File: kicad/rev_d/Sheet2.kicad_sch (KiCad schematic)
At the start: 216 parts, among them J10 vg_old, J5 external clock, J6 JUMPER, J8 JUMPER, J9 JUMPER, Q2 QUARTZ, Q3 QUARTZ32768, U1 74HCT1G04, X10 ST-214C, X11 KEYB-MOUSE, X12 IDC20, X13 USB_C, X14 AAFP/AC97 audio, X15 PLB2-2, X16 PLB1-4I, X17 PLB1-4I, X18 PLB1-4I, X19 AVR pgm conn, X20 PLB1-4I, X4 IDC10M, X5 IDC10M, X6 RS232_9

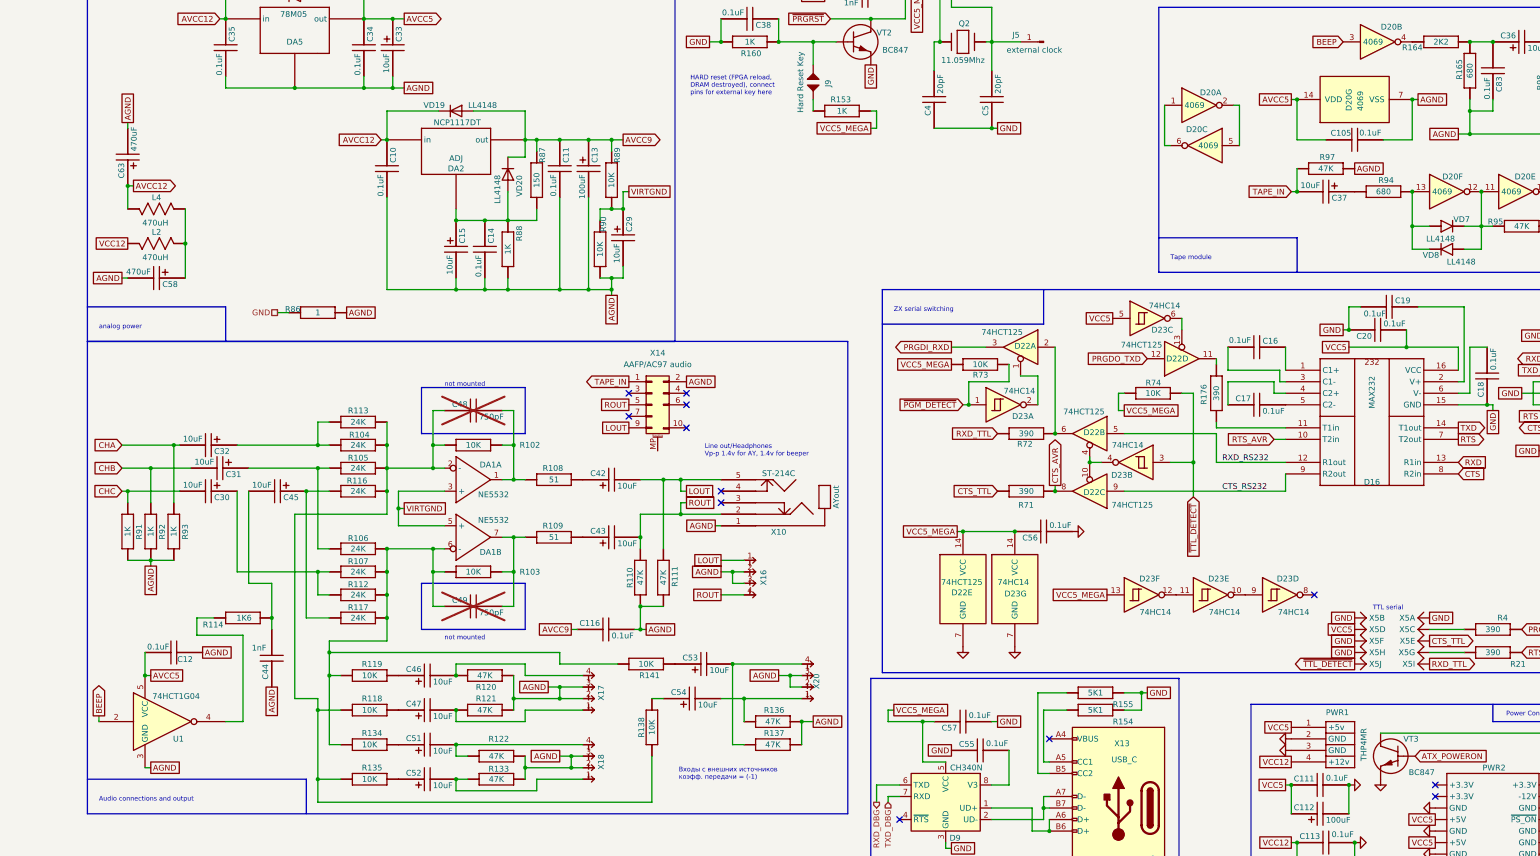
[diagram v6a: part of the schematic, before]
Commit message: pentevo: rev D: remove AGND, use GND instead
git-svn-id: svn://localhost/local-pentevo@1211 c6c76956-fad2-4150-a3a9-ea0a427205ba
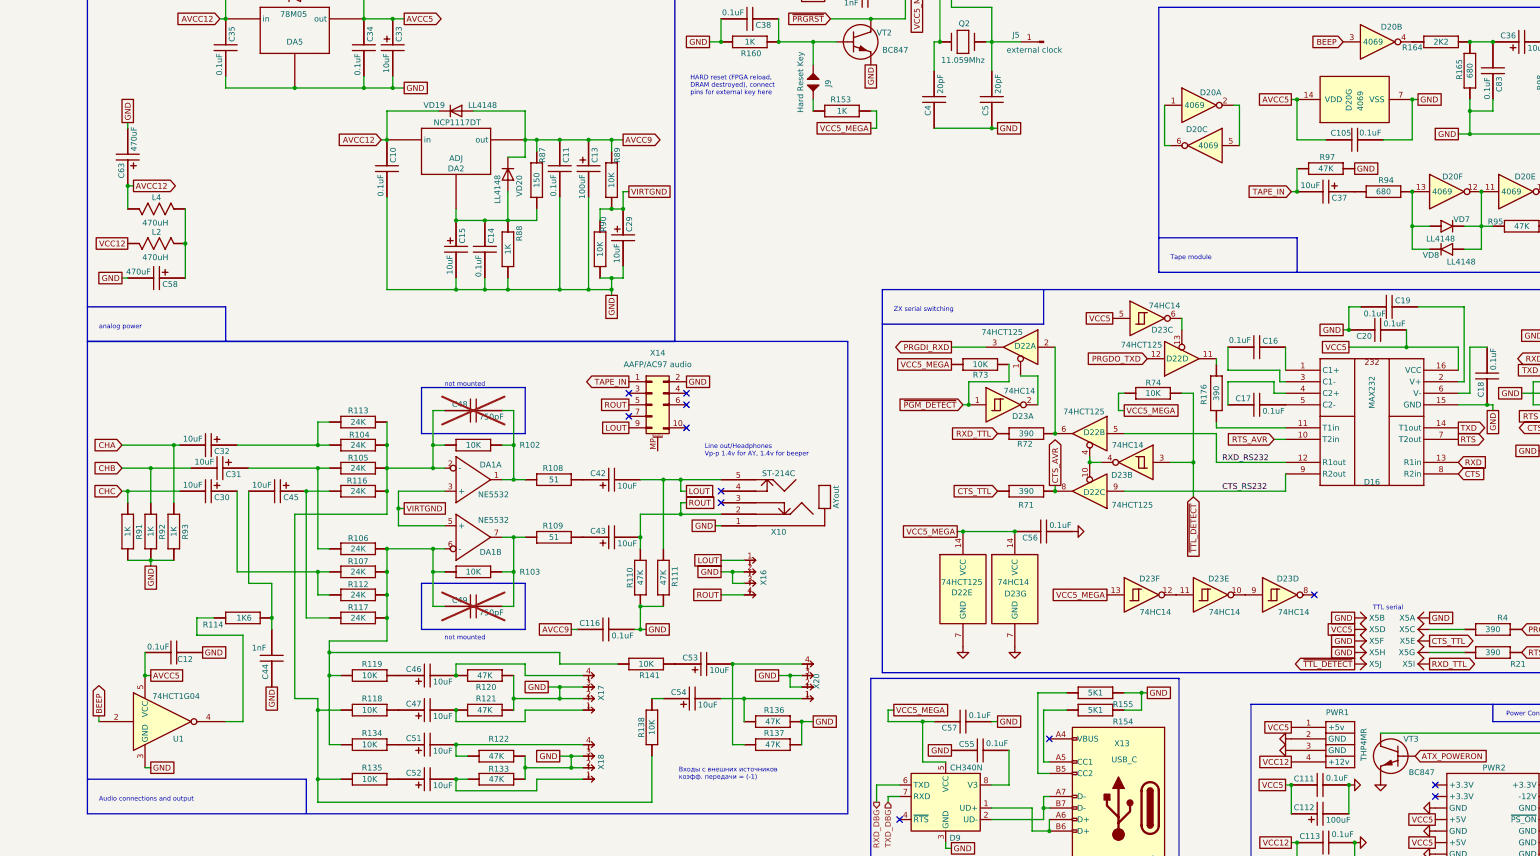
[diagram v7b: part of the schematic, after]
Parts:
- removed R86: 1, R-CHIP, symbol eva-altium-import:Sheet2_0_RESCHIP
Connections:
- net AGND is gone; now on net GND: C10.2, C105.2, C11.2, C116.2, C12.1, C13.2, C14.2, C15.2, C29.2, C33.2, C34.2, C35.2, C44.1, C58.2, C63.2, C83.1, D20.7 (VSS), DA5.2, R110.1 (i/o), R111.1 (i/o), R120.1 (i/o), R121.1 (i/o), R122.1 (i/o), R133.1 (i/o), R136.1 (i/o), R137.1 (i/o), R165.2 (i/o1), R88.1 (i/o), R90.1 (i/o), R91.1 (i/o), R92.1 (i/o), R93.1 (i/o), R97.1 (i/o), R98.1 (i/o), U1.3 (GND), X10.1, X14.2 (Pin_2), X15.2, X15.4 (2), X16.2 (I/O2), X16.3 (I/O3), X17.2 (I/O2), X17.3 (I/O3), X18.2 (I/O2), X18.3 (I/O3), X20.2 (I/O2), X20.3 (I/O3)
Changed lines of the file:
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@@
 	(wire
 		(pts
-			(xy 123.19 273.05) (xy 125.73 273.05)
-		)
-		(stroke
-			(width 0)
-			(type default)
-		)
-	)
-	(wire
-		(pts
 			(xy 284.48 88.9) (xy 284.48 96.52)
 		)
@@
 		)
 	)
-	(global_label "AGND"
+	(global_label "GND"
 		(shape passive)
 		(at 185.42 370.84 180)
@@
 		)
 		(property "Intersheetrefs" "${INTERSHEET_REFS}"
-			(at 178.587 370.84 0)
+			(at 179.6756 370.84 0)
 			(effects
 				(font
@@
 		)
 	)
-	(global_label "AGND"
+	(global_label "GND"
 		(shape passive)
 		(at 219.71 320.04 180)
@@
 		)
 		(property "Intersheetrefs" "${INTERSHEET_REFS}"
-			(at 212.877 320.04 0)
+			(at 213.9656 320.04 0)
 			(effects
 				(font
@@
 		)
 	)
-	(global_label "AGND"
+	(global_label "GND"
 		(shape passive)
 		(at 360.68 241.3 0)
@@
 		)
 		(property "Intersheetrefs" "${INTERSHEET_REFS}"
-			(at 367.513 241.3 0)
+			(at 366.4244 241.3 0)
 			(effects
 				(font
@@
 		)
 	)
-	(global_label "AGND"
+	(global_label "GND"
 		(shape passive)
 		(at 374.65 226.06 0)
@@
 		)
 		(property "Intersheetrefs" "${INTERSHEET_REFS}"
-			(at 381.483 226.06 0)
+			(at 380.3944 226.06 0)
 			(effects
 				(font
@@
 		)
 	)
-	(global_label "AGND"
-		(shape passive)
-		(at 138.43 273.05 0)
-		(fields_autoplaced yes)
-		(effects
-			(font
-				(size 1.27 1.27)
-			)
-			(justify left)
-		)
-		(property "Intersheetrefs" "${INTERSHEET_REFS}"
-			(at 145.263 273.05 0)
-			(effects
-				(font
-					(size 1.27 1.27)
-				)
-				(justify left)
-				(hide yes)
-			)
-		)
-	)
 	(global_label "PRGDO_TXD"
 		(shape input)
@@
 		)
 	)
-	(global_label "AGND"
+	(global_label "GND"
 		(shape passive)
 		(at 95.25 328.93 270)
@@
 		)
 		(property "Intersheetrefs" "${INTERSHEET_REFS}"
-			(at 95.25 335.763 90)
+			(at 95.25 334.6744 90)
 			(effects
 				(font
@@
 		)
 	)
-	(global_label "AGND"
+	(global_label "GND"
 		(shape passive)
 		(at 90.17 231.14 90)
@@
 		)
 		(property "Intersheetrefs" "${INTERSHEET_REFS}"
-			(at 90.17 224.307 90)
+			(at 90.17 225.3956 90)
 			(effects
 				(font
@@
 		)
 	)
-	(global_label "AGND"
+	(global_label "GND"
 		(shape passive)
 		(at 220.98 330.2 180)
@@
 		)
 		(property "Intersheetrefs" "${INTERSHEET_REFS}"
-			(at 214.147 330.2 0)
+			(at 215.2356 330.2 0)
 			(effects
 				(font
@@
 		)
 	)
-	(global_label "AGND"
+	(global_label "GND"
 		(shape passive)
 		(at 95.25 373.38 0)
@@
 		)
 		(property "Intersheetrefs" "${INTERSHEET_REFS}"
-			(at 102.083 373.38 0)
+			(at 100.9944 373.38 0)
 			(effects
 				(font
@@
 		)
 	)
-	(global_label "AGND"
+	(global_label "GND"
 		(shape passive)
 		(at 182.88 355.6 180)
@@
 		)
 		(property "Intersheetrefs" "${INTERSHEET_REFS}"
-			(at 176.047 355.6 0)
+			(at 177.1356 355.6 0)
 			(effects
 				(font
@@
 		)
 	)
-	(global_label "AGND"
+	(global_label "GND"
 		(shape passive)
 		(at 204.47 342.9 0)
@@
 		)
 		(property "Intersheetrefs" "${INTERSHEET_REFS}"
-			(at 211.303 342.9 0)
+			(at 210.2144 342.9 0)
 			(effects
 				(font
@@
 		)
 	)
-	(global_label "AGND"
+	(global_label "GND"
 		(shape passive)
 		(at 241.3 363.22 0)
@@
 		)
 		(property "Intersheetrefs" "${INTERSHEET_REFS}"
-			(at 248.133 363.22 0)
+			(at 247.0444 363.22 0)
 			(effects
 				(font
@@
 		)
 	)
-	(global_label "AGND"
+	(global_label "GND"
 		(shape passive)
 		(at 121.92 355.6 270)
@@
 		)
 		(property "Intersheetrefs" "${INTERSHEET_REFS}"
-			(at 121.92 362.433 90)
+			(at 121.92 361.3444 90)
 			(effects
 				(font
@@
 		)
 	)
-	(global_label "AGND"
+	(global_label "GND"
 		(shape passive)
 		(at 383.54 233.68 180)
@@
 		)
 		(property "Intersheetrefs" "${INTERSHEET_REFS}"
-			(at 376.707 233.68 0)
+			(at 377.7956 233.68 0)
 			(effects
 				(font
@@
 		)
 	)
-	(global_label "AGND"
+	(global_label "GND"
 		(shape passive)
 		(at 151.13 223.52 0)
@@
 		)
 		(property "Intersheetrefs" "${INTERSHEET_REFS}"
-			(at 157.963 223.52 0)
+			(at 156.8744 223.52 0)
 			(effects
 				(font
@@
 		)
 	)
-	(global_label "AGND"
+	(global_label "GND"
 		(shape passive)
 		(at 88.9 265.43 180)
@@
 		)
 		(property "Intersheetrefs" "${INTERSHEET_REFS}"
-			(at 82.067 265.43 0)
+			(at 83.1556 265.43 0)
 			(effects
 				(font
@@
 		)
 	)
-	(global_label "AGND"
+	(global_label "GND"
 		(shape passive)
 		(at 106.68 347.98 0)
@@
 		)
 		(property "Intersheetrefs" "${INTERSHEET_REFS}"
-			(at 113.513 347.98 0)
+			(at 112.4244 347.98 0)
 			(effects
 				(font
@@
 		)
 	)
-	(global_label "AGND"
+	(global_label "GND"
 		(shape passive)
 		(at 233.68 353.06 180)
@@
 		)
 		(property "Intersheetrefs" "${INTERSHEET_REFS}"
-			(at 226.847 353.06 0)
+			(at 227.9356 353.06 0)
 			(effects
 				(font
@@
 		)
 	)
-	(global_label "AGND"
+	(global_label "GND"
 		(shape passive)
 		(at 196.85 269.24 270)
@@
 		)
 		(property "Intersheetrefs" "${INTERSHEET_REFS}"
-			(at 196.85 276.073 90)
+			(at 196.85 274.9844 90)
 			(effects
 				(font
@@
 		)
 	)
-	(global_label "AGND"
+	(global_label "GND"
 		(shape passive)
 		(at 213.36 288.29 0)
@@
 		)
 		(property "Intersheetrefs" "${INTERSHEET_REFS}"
-			(at 220.193 288.29 0)
+			(at 219.1044 288.29 0)
 			(effects
 				(font
@@
 		)
 	)
-	(hierarchical_label "GND"
-		(shape passive)
-		(at 123.19 273.05 180)
-		(fields_autoplaced yes)
-		(effects
-			(font
-				(size 1.27 1.27)
-			)
-			(justify right)
-		)
-	)
 	(hierarchical_label "TXD_DBG"
 		(shape input)
@@
 					(unit 1)
 				)
-			)
-		)
-	)
-	(symbol
-		(lib_id "eva-altium-import:Sheet2_0_RESCHIP")
-		(at 125.73 273.05 0)
-		(unit 1)
-		(exclude_from_sim no)
-		(in_bom yes)
-		(on_board yes)
-		(dnp no)
-		(property "Reference" "R86"
-			(at 128.27 273.05 0)
-			(effects
-				(font
-					(size 1.27 1.27)
-				)
-				(justify right bottom)
-			)
-		)
-		(property "Value" "1"
-			(at 132.08 273.05 0)
-			(effects
-				(font
-					(size 1.27 1.27)
-				)
-			)
-		)
-		(property "Footprint" "R-CHIP"
-			(at 125.73 273.05 0)
-			(effects
-				(font
-					(size 1.27 1.27)
-				)
-				(hide yes)
-			)
-		)
-		(property "Datasheet" ""
-			(at 125.73 273.05 0)
-			(effects
-				(font
-					(size 1.27 1.27)
-				)
-				(hide yes)
-			)
-		)
-		(property "Description" "RESCHIP"
-			(at 125.73 273.05 0)
-			(effects
-				(font
-					(size 1.27 1.27)
-				)
-				(hide yes)
-			)
-		)
-		(pin "2"
-		)
-		(pin "1"
-		)
-		(instances
-			(project ""
-				(path "/ab605654-a730-497b-9e09-9b351f74b935/31d5864f-06ec-4c73-9256-780a6880087d"
-					(reference "R86")
-					(unit 1)
-				)

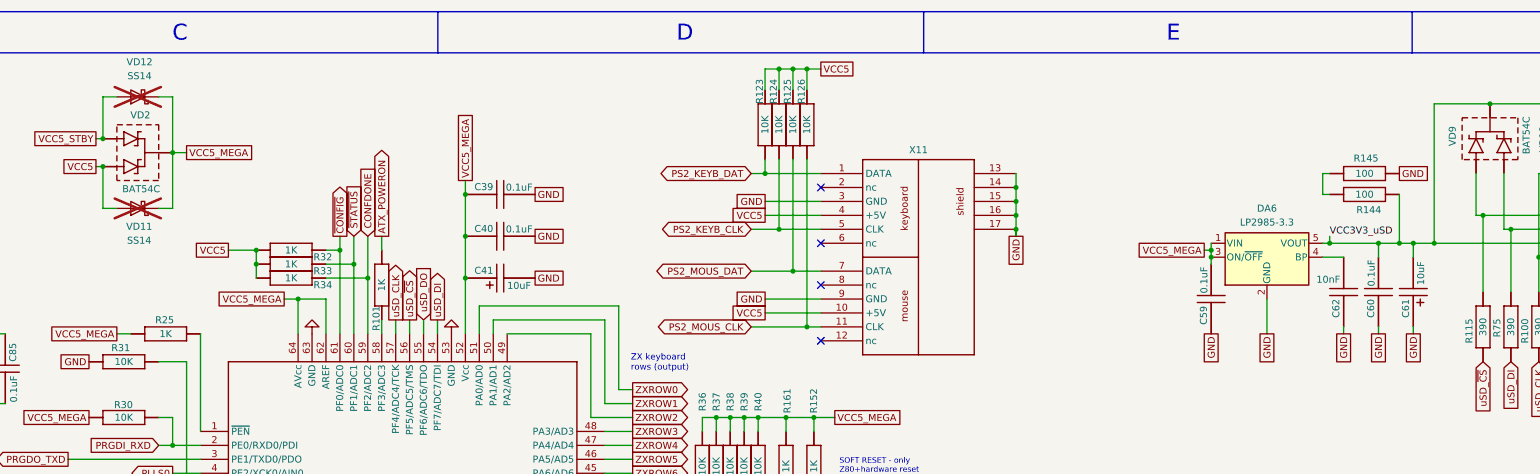
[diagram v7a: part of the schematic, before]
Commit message: pentevo: rev D: fix uSD card capacitors, replace 2 series resistors with single one, make BAT54c for AVR 'do not populate' instead of SS14, replace 10uF for AVR from tantalum to X7R
git-svn-id: svn://localhost/local-pentevo@1213 c6c76956-fad2-4150-a3a9-ea0a427205ba
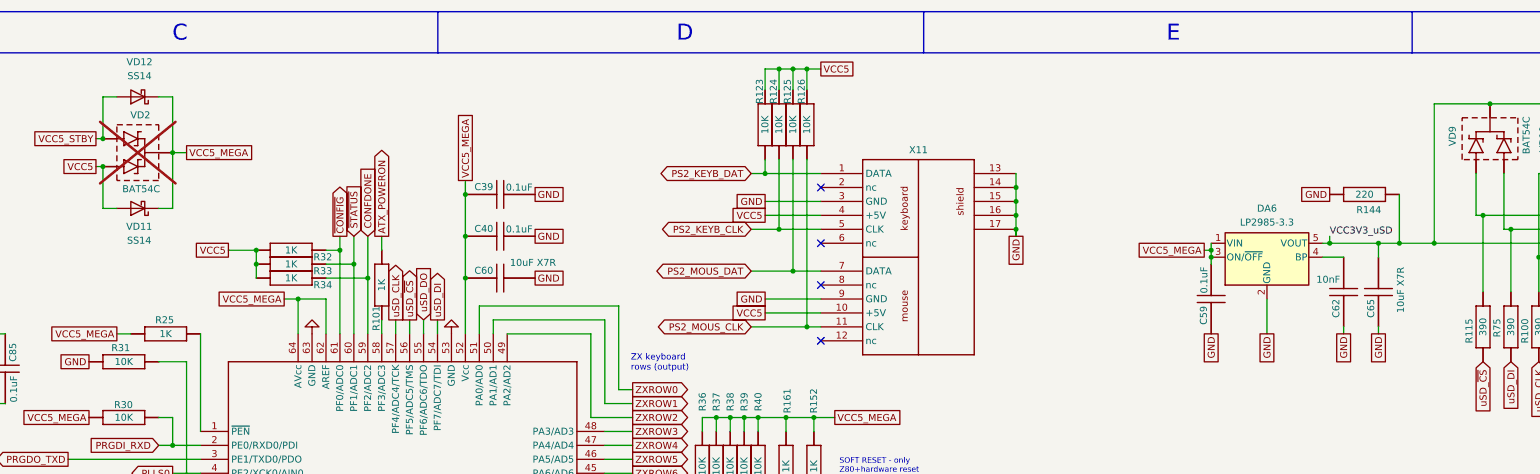
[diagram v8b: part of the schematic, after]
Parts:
- removed C41, C61: 10uF, EC-CHIP, symbol eva-altium-import:Sheet2_0_ECAPCHIP
- removed R145: 100, R-CHIP, symbol eva-altium-import:Sheet1_0_RESCHIP
- added C65: 10uF X7R, Capacitor_SMD:C_1206_3216Metric_Pad1.33x1.80mm_HandSolder, symbol eva-altium-import:Sheet2_0_CAPCHIP
- C60: value 0.1uF -> 10uF X7R; footprint C-CHIP -> Capacitor_SMD:C_1206_3216Metric_Pad1.33x1.80mm_HandSolder
- R144: value 100 -> 220
- VD11, VD12: now fitted
- VD2: now not fitted
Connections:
- net GND: now also C60.2, R144.2 (i/o1), C65.1; no longer C60.1
- net VCC3V3_uSD: now also C65.2; no longer C60.2
- net VCC5_MEGA: now also C60.1
